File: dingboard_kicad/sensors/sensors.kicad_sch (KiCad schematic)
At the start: 68 parts, among them J1 Bus_PCI_Express_x1, J2 TYPE-C-31-M-04, J3 Conn_01x02, U2 RP2040, U3 TPS2121RUXR, U4 W25Q128JVP, U5 BMP388, U6 LMR51430 1.1k FPWM, U7 TPS63070RNMR, U8 BNO055, U9 MCP25625T-E/ML, X1 ABM8-272-T3, Y1 ABS07-32.768KHZ-T, Y2 X322516MLB4SI

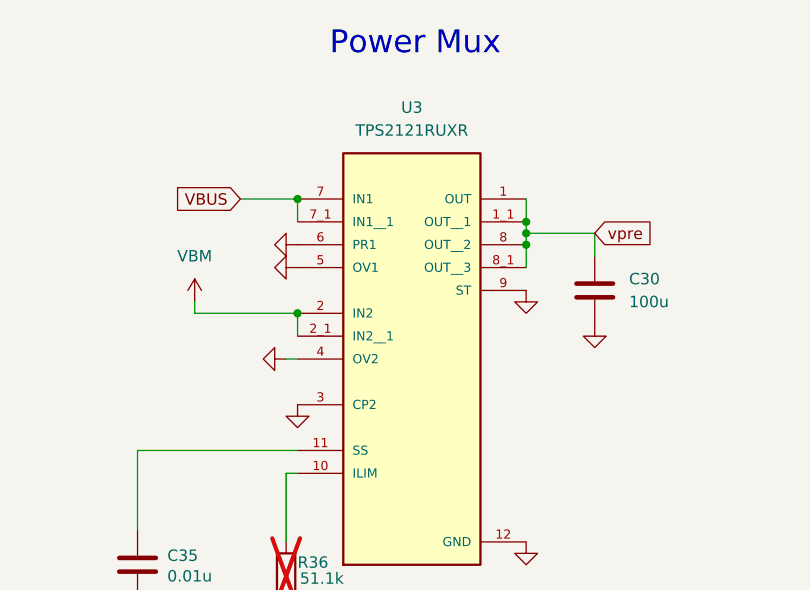
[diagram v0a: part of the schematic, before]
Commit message: add current estimation to BOM
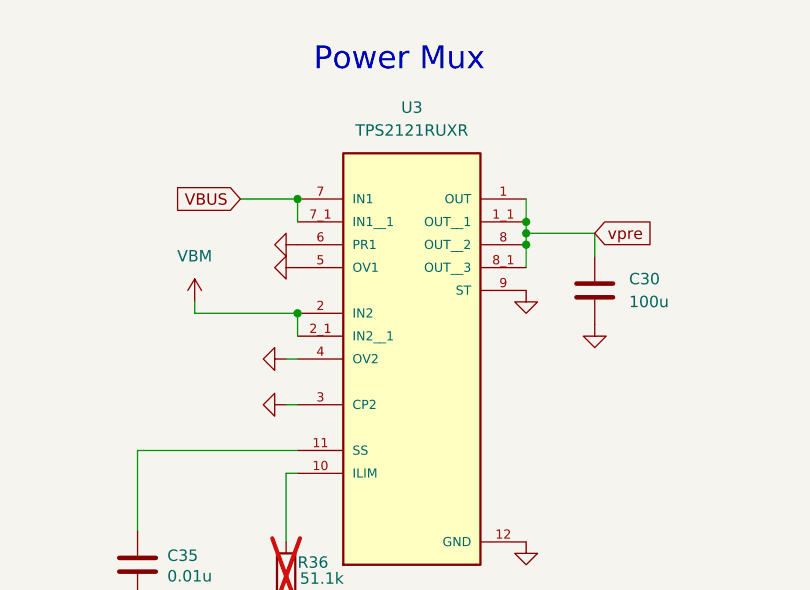
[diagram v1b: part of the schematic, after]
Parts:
- U2: max mA (none) -> 20mA
- U3: max mA (none) -> 500 uA
- U4: max mA (none) -> 25mA
- U5: info BMP288 -> BMP388; max mA (none) -> 800uA
- U6: info DC-DC Converter -> 3.3v Buck; max mA (none) -> 65uA
- U7: max mA (none) -> 103uA
- U8: max mA (none) -> 12.3mA
- U9: max mA (none) -> Con=10mA, Tra=70mA
- X1, Y2: max mA (none) -> 200 uW 3.3v
- Y1: max mA (none) -> 0.5 uW 3.3v
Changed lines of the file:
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@@
 	(wire
 		(pts
+			(xy 196.85 80.01) (xy 198.12 80.01)
+		)
+		(stroke
+			(width 0)
+			(type default)
+		)
+	)
+	(wire
+		(pts
 			(xy 474.98 261.62) (xy 474.98 278.13)
 		)
@@
 	(text "Power Mux"
 		(exclude_from_sim no)
-		(at 201.676 41.402 0)
+		(at 199.898 43.18 0)
 		(effects
 			(font
@@
 			)
 		)
+		(property "max mA" "200 uW 3.3v"
+			(at 180.34 245.11 0)
+			(effects
+				(font
+					(size 1.27 1.27)
+				)
+				(hide yes)
+			)
+		)
 		(pin "1"
 		)
@@
 			)
 		)
+		(property "max mA" "12.3mA"
+			(at 509.27 280.67 0)
+			(effects
+				(font
+					(size 1.27 1.27)
+				)
+				(hide yes)
+			)
+		)
 		(pin "17"
 		)
@@
 	(symbol
 		(lib_id "power:GND")
-		(at 198.12 80.01 0)
+		(at 196.85 80.01 270)
 		(unit 1)
 		(exclude_from_sim no)
@@
 		(fields_autoplaced yes)
 		(property "Reference" "#PWR030"
-			(at 198.12 86.36 0)
+			(at 190.5 80.01 0)
 			(effects
 				(font
@@
 		)
 		(property "Value" "GND"
-			(at 198.12 85.09 0)
+			(at 191.77 80.01 0)
 			(effects
 				(font
@@
 		)
 		(property "Footprint" ""
-			(at 198.12 80.01 0)
+			(at 196.85 80.01 0)
 			(effects
 				(font
@@
 		)
 		(property "Datasheet" ""
-			(at 198.12 80.01 0)
+			(at 196.85 80.01 0)
 			(effects
 				(font
@@
 		)
 		(property "Description" "Power symbol creates a global label with name \"GND\" , ground"
-			(at 198.12 80.01 0)
+			(at 196.85 80.01 0)
 			(effects
 				(font
@@
 			)
 		)
+		(property "max mA" "500 uA"
+			(at 210.82 72.39 0)
+			(effects
+				(font
+					(size 1.27 1.27)
+				)
+				(hide yes)
+			)
+		)
 		(pin "2_1"
 		)
@@
 			)
 		)
-		(property "info" "DC-DC Converter"
+		(property "info" "3.3v Buck"
 			(at 347.726 63.754 0)
 			(effects
@@
 			)
 		)
+		(property "max mA" "65uA"
+			(at 347.98 69.85 0)
+			(effects
+				(font
+					(size 1.27 1.27)
+				)
+				(hide yes)
+			)
+		)
 		(pin "1"
 		)
@@
 			)
 		)
+		(property "max mA" "200 uW 3.3v"
+			(at 430.53 346.71 0)
+			(effects
+				(font
+					(size 1.27 1.27)
+				)
+				(hide yes)
+			)
+		)
 		(pin "1"
 		)
@@
 			)
 		)
+		(property "max mA" "25mA"
+			(at 135.89 175.26 0)
+			(effects
+				(font
+					(size 1.27 1.27)
+				)
+				(hide yes)
+			)
+		)
 		(pin "8"
 		)
@@
 			)
 		)
+		(property "max mA" "20mA"
+			(at 350.52 231.14 0)
+			(effects
+				(font
+					(size 1.27 1.27)
+				)
+				(hide yes)
+			)
+		)
 		(pin "16"
 		)
@@
 			)
 		)
+		(property "max mA" "Con=10mA, Tra=70mA"
+			(at 346.71 330.2 0)
+			(effects
+				(font
+					(size 1.27 1.27)
+				)
+				(hide yes)
+			)
+		)
 		(pin "14"
 		)
@@
 			)
 		)
+		(property "max mA" "0.5 uW 3.3v"
+			(at 537.21 274.32 0)
+			(effects
+				(font
+					(size 1.27 1.27)
+				)
+				(hide yes)
+			)
+		)
 		(pin "2"
 		)
@@
 			)
 		)
+		(property "max mA" "103uA"
+			(at 213.36 340.36 0)
+			(effects
+				(font
+					(size 1.27 1.27)
+				)
+				(hide yes)
+			)
+		)
 		(pin "15"
 		)
@@
 			)
 		)
-		(property "info" "BMP288"
+		(property "info" "BMP388"
 			(at 494.03 71.12 0)
 			(effects
@@
 			(at 494.03 71.12 0)
 			(effects
+				(font
+					(size 1.27 1.27)
+				)
+				(hide yes)
+			)
+		)
+		(property "max mA" "800uA"
+			(at 494.03 71.12 0)
+			(effects

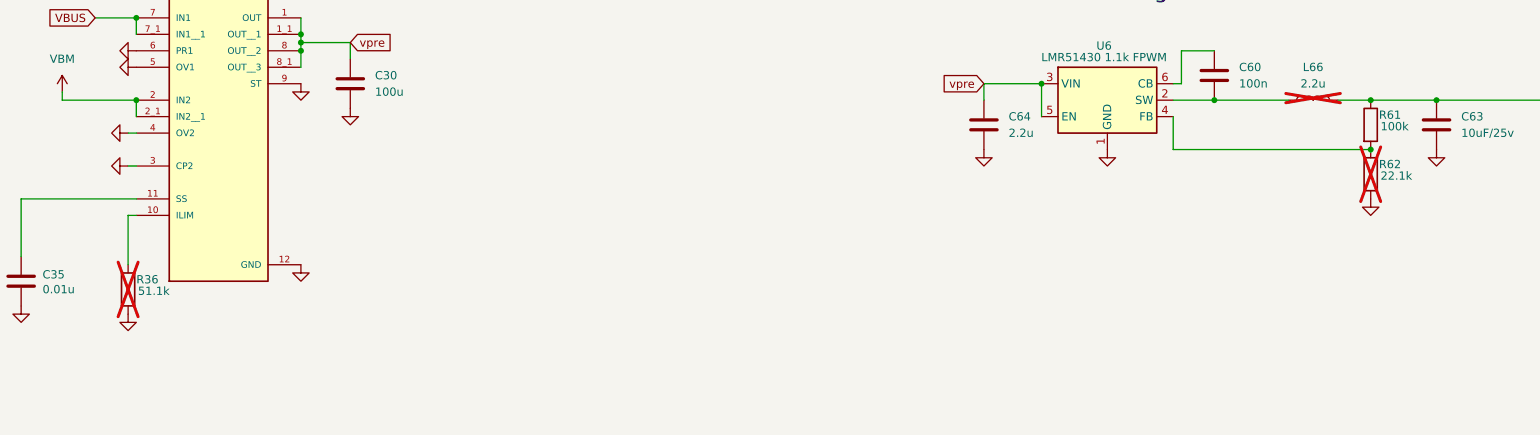
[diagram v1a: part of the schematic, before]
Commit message: switch to Sonic Avionics
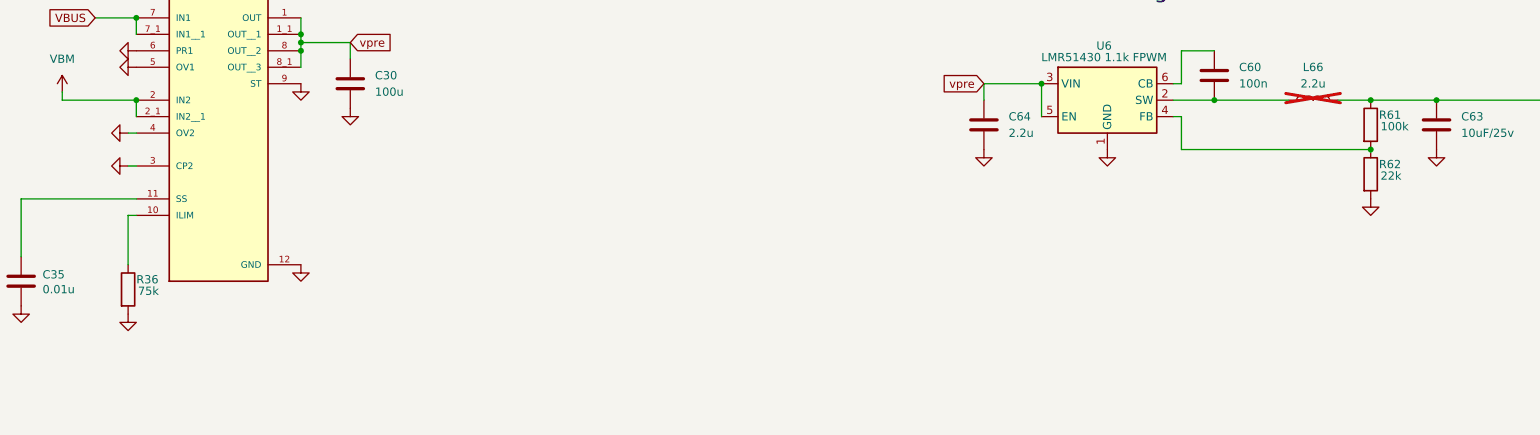
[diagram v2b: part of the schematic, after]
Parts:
- R36: value 51.1k -> 75k; Digikey Link https://www.digikey.ca/en/products/detail/yageo/RC0603FR-07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 -> (none); JLC Link (none) -> https://jlcpcb.com/partdetail/23969-0603WAF7502T5E/C23242; LCSC Part # C23072 -> C23242; basic? no -> yes; info 51.1k ohm -> 75k ohm; price $0.16 -> C$0.0013; now fitted
- R62: value 22.1k -> 22k; info 22.1k ohm -> 22k ohm; now fitted
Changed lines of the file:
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@@
 	(wire
 		(pts
-			(xy 358.14 77.47) (xy 388.62 77.47)
+			(xy 359.41 77.47) (xy 388.62 77.47)
 		)
 		(stroke
@@
 	(wire
 		(pts
+			(xy 359.41 72.39) (xy 358.14 72.39)
+		)
+		(stroke
+			(width 0)
+			(type default)
+		)
+	)
+	(wire
+		(pts
 			(xy 369.57 168.91) (xy 369.57 167.64)
 		)
@@
 	(wire
 		(pts
-			(xy 358.14 77.47) (xy 358.14 72.39)
+			(xy 359.41 77.47) (xy 359.41 72.39)
 		)
 		(stroke
@@
 		(in_bom yes)
 		(on_board yes)
-		(dnp yes)
+		(dnp no)
 		(property "Reference" "R62"
 			(at 389.89 79.756 0)
@@
 			)
 		)
-		(property "Value" "22.1k"
+		(property "Value" "22k"
 			(at 390.144 81.534 0)
 			(effects
@@
 			)
 		)
-		(property "info" "22.1k ohm"
+		(property "info" "22k ohm"
 			(at 388.62 81.28 0)
 			(effects
@@
 		(in_bom yes)
 		(on_board yes)
-		(dnp yes)
+		(dnp no)
 		(property "Reference" "R36"
 			(at 198.12 97.536 0)
@@
 			)
 		)
-		(property "Value" "51.1k"
+		(property "Value" "75k"
 			(at 198.374 99.314 0)
 			(effects
@@
 			)
 		)
-		(property "LCSC Part #" "C23072"
+		(property "LCSC Part #" "C23242"
 			(at 196.85 99.06 0)
 			(effects
@@
 			)
 		)
-		(property "basic?" "no"
+		(property "basic?" "yes"
 			(at 196.85 99.06 0)
 			(effects
@@
 			)
 		)
-		(property "info" "51.1k ohm"
+		(property "info" "75k ohm"
 			(at 196.85 99.06 0)
 			(effects
@@
 			)
 		)
-		(property "price" "$0.16"
+		(property "price" " C$0.0013 "
+			(at 196.85 99.06 0)
+			(effects
+				(font
+					(size 1.27 1.27)
+				)
+				(hide yes)
+			)
+		)
+		(property "Digikey Link" ""
 			(at 196.85 99.06 0)
 			(effects
@@
 			)
 		)
-		(property "Digikey Link" "https://www.digikey.ca/en/products/detail/yageo/RC0603FR-0751K1L/727284"
+		(property "JLC Link" "https://jlcpcb.com/partdetail/23969-0603WAF7502T5E/C23242"
 			(at 196.85 99.06 0)
 			(effects

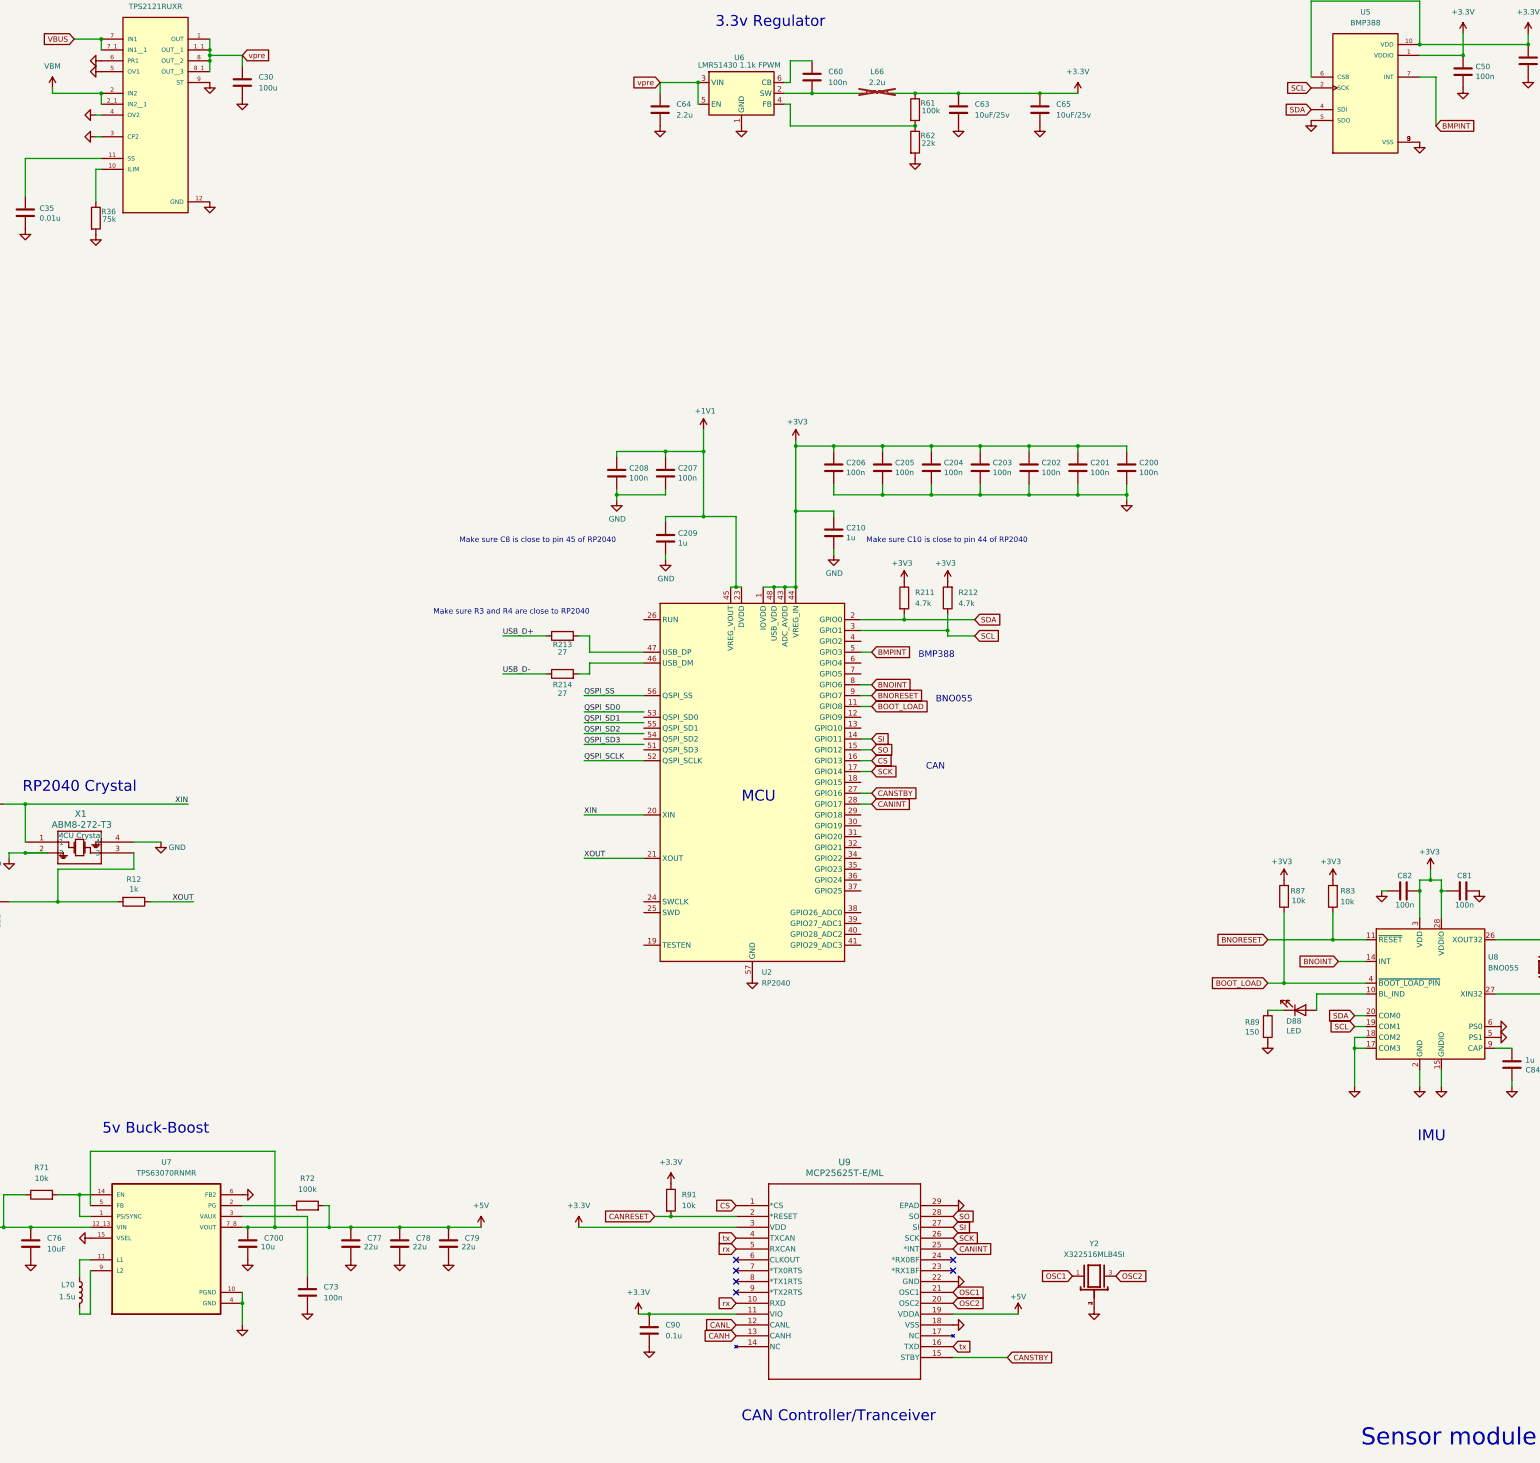
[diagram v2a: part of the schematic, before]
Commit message: update capacitors for basic assembly, export new schematic PDF
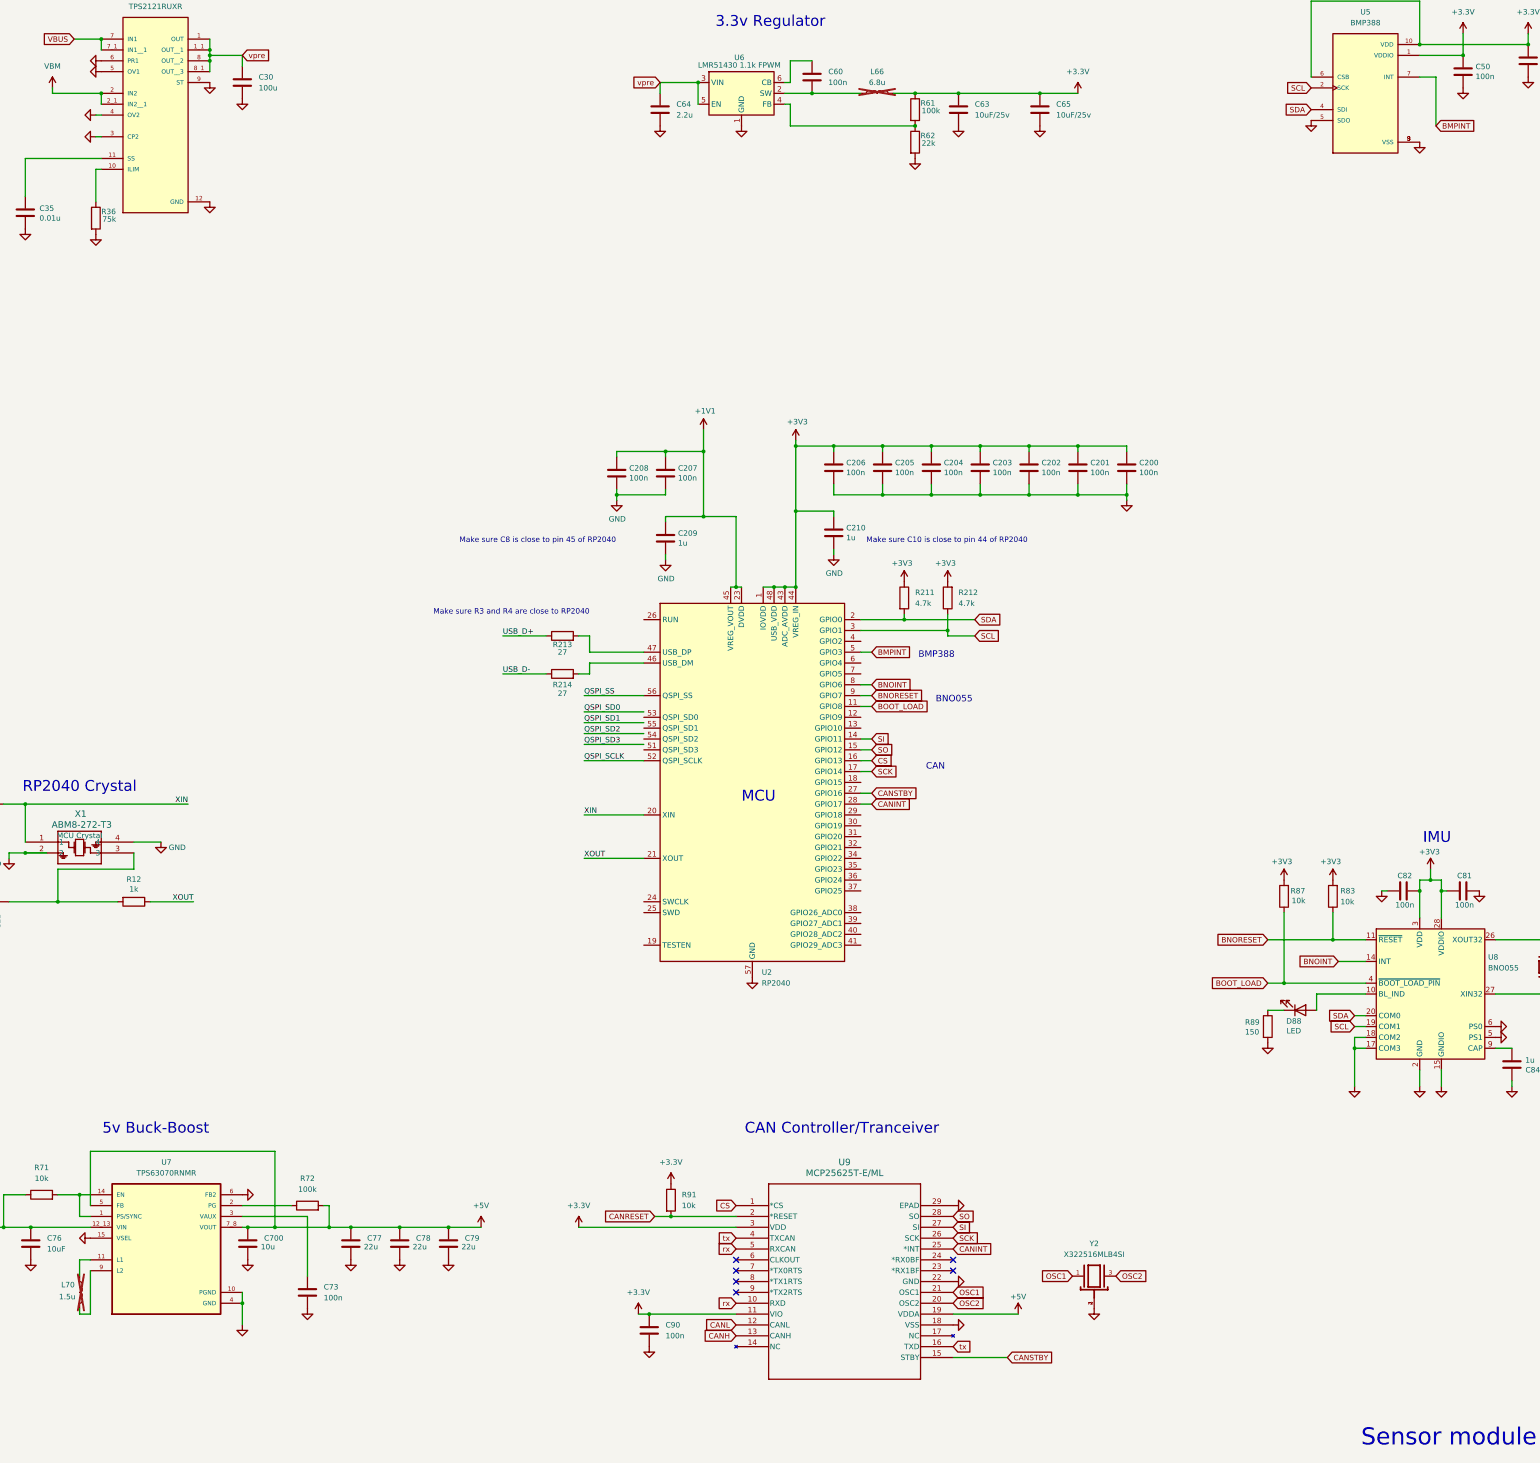
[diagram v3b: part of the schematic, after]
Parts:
- C90: value 0.1u -> 100n; footprint (none) -> Capacitor_SMD:C_0402_1005Metric; JLC Link (none) -> https://jlcpcb.com/partdetail/291005-CL05B104KB54PNC/C307331; LCSC Part # (none) -> C307331; basic? (none) -> yes; info (none) -> 100nF Cap; price (none) -> C$0.0077
- L66: value 2.2u -> 6.8u; footprint Inductor_SMD:L_0603_1608Metric -> (none); Digikey Link (none) -> https://www.digikey.ca/en/products/detail/tdk-corporation/V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; JLC Link (none) -> https://jlcpcb.com/partdetail/Tdk-VLS6045EX6R8M/C415364; LCSC Part # (none) -> C415364; basic? (none) -> no; info 2.2uH -> 6.8uH; notes (none) -> VLS6045EX-6R8M; price (none) -> C$0.1397
- L70: footprint Inductor_SMD:L_0603_1608Metric -> (none); Digikey Link (none) -> https://www.digikey.ca/en/products/detail/coilcraft/XFL4020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; JLC Link (none) -> https://jlcpcb.com/partdetail/Coilcraft-XFL4020152MEC/C3033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; LCSC Part # (none) -> C3033018; basic? (none) -> no; info (none) -> 1.5uH; notes (none) -> XFL4020-152MEC; price (none) -> C$1.3436; now not fitted
- R36: notes (none) -> 0603 is only basic 75k; price C$0.0013 -> C$0.0013
- R62: footprint Resistor_SMD:R_0603_1608Metric -> Resistor_SMD:R_0402_1005Metric; Digikey Link https://www.digikey.ca/en/products/detail/stackpole-electro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 -> (none); JLC Link (none) -> https://jlcpcb.com/partdetail/26511-0402WGF2202TCE/C25768; LCSC Part # C25961 -> C25768; basic? no -> yes; price $0.16 -> C$0.0007
- U2: Current Draw (none) -> 20mA; max mA 20mA -> (none)
- U3: Current Draw (none) -> 500 uA; max mA 500 uA -> (none)
- U4: Current Draw (none) -> 25mA; max mA 25mA -> (none)
- U5: Current Draw (none) -> 800uA; max mA 800uA -> (none)
- U6: Current Draw (none) -> 65uA; max mA 65uA -> (none)
- U7: Current Draw (none) -> 103uA; max mA 103uA -> (none)
- U8: Current Draw (none) -> 12.3mA; max mA 12.3mA -> (none)
- U9: Current Draw (none) -> Con=10mA, Tra=70mA; max mA Con=10mA, Tra=70mA -> (none)
- X1, Y2: Current Draw (none) -> 200 uW 3.3v; max mA 200 uW 3.3v -> (none)
- Y1: Current Draw (none) -> 0.5 uW 3.3v; max mA 0.5 uW 3.3v -> (none)
